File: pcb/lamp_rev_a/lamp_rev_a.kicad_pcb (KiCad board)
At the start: 4 copper layers, 100 x 80 mm, 0 parts

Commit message: Materialize LAMP Rev A KiCad board
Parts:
- added C1: 22uF, lcsc:C1206, F.Cu at (26.0, 8.00)
- added C10: 100nF, lcsc:C0603, F.Cu at (42.0, 14.0)
- added C11: 100nF, lcsc:C0603, F.Cu at (47.0, 14.0)
- added C12: 100nF, lcsc:C0603, F.Cu at (50.0, 51.0)
- added C13: 100nF, lcsc:C0603, F.Cu at (54.0, 51.0)
- added C14: 100nF, lcsc:C0603, F.Cu at (44.0, 55.0)
- added C15: 100nF, lcsc:C0603, F.Cu at (68.0, 15.0)
- added C16: 100nF, lcsc:C0603, F.Cu at (9.00, 57.0)
- added C17: 100nF, lcsc:C0603, F.Cu at (21.0, 57.0)
- added C18: 100nF, lcsc:C0603, F.Cu at (33.0, 57.0)
- added C19: 100nF, lcsc:C0603, F.Cu at (45.0, 68.0)
- added C2: 22uF, lcsc:C1206, F.Cu at (38.0, 8.00)
- added C20: 100nF, lcsc:C0603, F.Cu at (69.0, 57.0)
- added C21: 100nF, lcsc:C0603, F.Cu at (93.0, 57.0)
- added C3: 22uF, lcsc:C1206, F.Cu at (48.0, 12.0)
- added C4: 22uF, lcsc:C1206, F.Cu at (84.0, 6.00)
- added C5: 10pF, lcsc:C0603, F.Cu at (47.0, 62.0)
- added C6: 100nF, lcsc:C0603, F.Cu at (18.0, 14.0)
- added C7: 100nF, lcsc:C0603, F.Cu at (22.0, 14.0)
- added C8: 100nF, lcsc:C0603, F.Cu at (27.0, 18.0)
- added C9: 100nF, lcsc:C0603, F.Cu at (17.0, 9.00)
- added D1: SS34, lcsc:SMA_L4.3-W2.6-LS5.2-RD, F.Cu at (32.0, 8.00)
- added D10: SMBJ18A, lcsc:SMB_L4.6-W3.6-LS5.3-RD, F.Cu at (75.0, 25.0)
- added D11: KT-0603R, lcsc:LED0603-RD, F.Cu at (10.0, 30.0)
- added D12: KT-0603R, lcsc:LED0603-RD, F.Cu at (15.0, 30.0)
- added D13: SS34, lcsc:SMA_L4.3-W2.6-LS5.2-RD, F.Cu at (84.0, 12.0)
- added D2: KT-0603R, lcsc:LED0603-RD, F.Cu at (8.00, 54.0)
- added D3: KT-0603R, lcsc:LED0603-RD, F.Cu at (20.0, 54.0)
- added D4: KT-0603R, lcsc:LED0603-RD, F.Cu at (32.0, 54.0)
- added D5: KT-0603R, lcsc:LED0603-RD, F.Cu at (44.0, 54.0)
- added D6: KT-0603R, lcsc:LED0603-RD, F.Cu at (56.0, 54.0)
- added D7: KT-0603R, lcsc:LED0603-RD, F.Cu at (68.0, 54.0)
- added D8: KT-0603R, lcsc:LED0603-RD, F.Cu at (80.0, 54.0)
- added D9: KT-0603R, lcsc:LED0603-RD, F.Cu at (92.0, 54.0)
- added F1: SMD2920-300C-36V, lcsc:FUSE2920, F.Cu at (82.0, 20.0)
- added J1: TYPE-C 3.1 MT 16P, lcsc:USB-C-SMD_TYPE-C-USB-4, F.Cu at (7.00, 7.00)
- added J2: DC-005-5A-2.0, lcsc:DC-IN-TH_DC-005-5A-2.0, F.Cu at (92.0, 8.00)
- added J3: DB128H-5.08-2P-BK-S, lcsc:TERM-BLOCK-5.08-2P, F.Cu at (92.0, 25.0)
- added PD1: SFH2704, lcsc:PHOTODIODE-SMD-2X1.8, F.Cu at (8.00, 70.0)
- added PD2: SFH2704, lcsc:PHOTODIODE-SMD-2X1.8, F.Cu at (20.0, 70.0)
- added PD3: SFH2704, lcsc:PHOTODIODE-SMD-2X1.8, F.Cu at (32.0, 70.0)
- added PD4: SFH2704, lcsc:PHOTODIODE-SMD-2X1.8, F.Cu at (44.0, 70.0)
- added PD5: SFH2704, lcsc:PHOTODIODE-SMD-2X1.8, F.Cu at (56.0, 70.0)
- added PD6: SFH2704, lcsc:PHOTODIODE-SMD-2X1.8, F.Cu at (68.0, 70.0)
- added PD7: SFH2704, lcsc:PHOTODIODE-SMD-2X1.8, F.Cu at (80.0, 70.0)
- added PD8: SFH2704, lcsc:PHOTODIODE-SMD-2X1.8, F.Cu at (92.0, 70.0)
- added Q1: AO3400A, lcsc:SOT-23-3_L2.9-W1.3-P1.90-LS2.4-BR, F.Cu at (75.0, 17.0)
- added Q2: MMBT3904, lcsc:SOT-23-3_L2.9-W1.3-P1.90-LS2.4-BR, F.Cu at (8.00, 48.0)
- added Q3: MMBT3904, lcsc:SOT-23-3_L2.9-W1.3-P1.90-LS2.4-BR, F.Cu at (20.0, 48.0)
- added Q4: MMBT3904, lcsc:SOT-23-3_L2.9-W1.3-P1.90-LS2.4-BR, F.Cu at (32.0, 48.0)
- added Q5: MMBT3904, lcsc:SOT-23-3_L2.9-W1.3-P1.90-LS2.4-BR, F.Cu at (44.0, 48.0)
- added Q6: MMBT3904, lcsc:SOT-23-3_L2.9-W1.3-P1.90-LS2.4-BR, F.Cu at (56.0, 48.0)
- added Q7: MMBT3904, lcsc:SOT-23-3_L2.9-W1.3-P1.90-LS2.4-BR, F.Cu at (68.0, 48.0)
- added Q8: MMBT3904, lcsc:SOT-23-3_L2.9-W1.3-P1.90-LS2.4-BR, F.Cu at (80.0, 48.0)
- added Q9: MMBT3904, lcsc:SOT-23-3_L2.9-W1.3-P1.90-LS2.4-BR, F.Cu at (92.0, 48.0)
- added R1: 5.1k, lcsc:R0805, F.Cu at (12.0, 13.0)
- added R10: 100R, lcsc:R0805, F.Cu at (80.0, 51.0)
- added R11: 100R, lcsc:R0805, F.Cu at (92.0, 51.0)
- added R12: 1k, lcsc:R0805, F.Cu at (8.00, 46.0)
- added R13: 1k, lcsc:R0805, F.Cu at (20.0, 46.0)
- added R14: 1k, lcsc:R0805, F.Cu at (32.0, 46.0)
- added R15: 1k, lcsc:R0805, F.Cu at (44.0, 46.0)
- added R16: 1k, lcsc:R0805, F.Cu at (56.0, 46.0)
- added R17: 1k, lcsc:R0805, F.Cu at (68.0, 46.0)
- added R18: 1k, lcsc:R0805, F.Cu at (80.0, 46.0)
- added R19: 1k, lcsc:R0805, F.Cu at (92.0, 46.0)
- added R2: 5.1k, lcsc:R0805, F.Cu at (12.0, 15.0)
- added R20: 1k, lcsc:R0805, F.Cu at (10.0, 27.0)
- added R21: 1k, lcsc:R0805, F.Cu at (15.0, 27.0)
- added R22: 4.7k, lcsc:R0805, F.Cu at (29.0, 28.0)
- added R23: 4.7k, lcsc:R0805, F.Cu at (32.0, 28.0)
- added R24: 10k, lcsc:R0805, F.Cu at (26.0, 24.0)
- added R25: 10k, lcsc:R0805, F.Cu at (30.0, 24.0)
- added R26: 10k, lcsc:R0805, F.Cu at (57.0, 50.0)
- added R27: 10k, lcsc:R0805, F.Cu at (60.0, 50.0)
- added R28: 10k, lcsc:R0805, F.Cu at (65.0, 50.0)
- added R29: 10k, lcsc:R0805, F.Cu at (68.0, 50.0)
- added R3: 1M, lcsc:R0805, F.Cu at (43.0, 62.0)
- added R4: 100R, lcsc:R0805, F.Cu at (8.00, 51.0)
- added R5: 100R, lcsc:R0805, F.Cu at (20.0, 51.0)
- added R6: 100R, lcsc:R0805, F.Cu at (32.0, 51.0)
- added R7: 100R, lcsc:R0805, F.Cu at (44.0, 51.0)
- added R8: 100R, lcsc:R0805, F.Cu at (56.0, 51.0)
- added R9: 100R, lcsc:R0805, F.Cu at (68.0, 51.0)
- added TP_12V: +12V_RAW, lcsc:TESTPOINT_SMD_1.5MM, F.Cu at (98.0, 5.00)
- added TP_3V3: +3V3, lcsc:TESTPOINT_SMD_1.5MM, F.Cu at (50.0, 4.00)
- added TP_5V: +5V, lcsc:TESTPOINT_SMD_1.5MM, F.Cu at (38.0, 4.00)
- added TP_ADC: ADC_AIN1, lcsc:TESTPOINT_SMD_1.5MM, F.Cu at (40.0, 74.0)
- added TP_BOOT: ESP_GPIO0, lcsc:TESTPOINT_SMD_1.5MM, F.Cu at (22.0, 34.0)
- added TP_EN: ESP_EN, lcsc:TESTPOINT_SMD_1.5MM, F.Cu at (18.0, 34.0)
- added TP_GND: GND, lcsc:TESTPOINT_SMD_1.5MM, F.Cu at (5.00, 38.0)
- added TP_HEATER: HEATER_P, lcsc:TESTPOINT_SMD_1.5MM, F.Cu at (98.0, 30.0)
- added TP_HEATER_SUPPLY: HEATER_SUPPLY, lcsc:TESTPOINT_SMD_1.5MM, F.Cu at (88.0, 34.0)
- added TP_MUX: MUX_COM, lcsc:TESTPOINT_SMD_1.5MM, F.Cu at (45.0, 74.0)
- added TP_PWM: HEATER_PWM, lcsc:TESTPOINT_SMD_1.5MM, F.Cu at (64.0, 4.00)
- added TP_RX: UART_RX, lcsc:TESTPOINT_SMD_1.5MM, F.Cu at (30.0, 34.0)
- added TP_SCL: SCL, lcsc:TESTPOINT_SMD_1.5MM, F.Cu at (32.0, 34.0)
- added TP_SDA: SDA, lcsc:TESTPOINT_SMD_1.5MM, F.Cu at (28.0, 34.0)
- added TP_TX: UART_TX, lcsc:TESTPOINT_SMD_1.5MM, F.Cu at (26.0, 34.0)
- added TP_VBUS: VBUS, lcsc:TESTPOINT_SMD_1.5MM, F.Cu at (12.0, 4.00)
- added U1: ESP32-S3-WROOM-1-N8, lcsc:WIFIM-SMD_ESP32-S3-WROOM-1-N8, F.Cu at (22.0, 20.0)
- added U2: USBLC6-2SC6, lcsc:SOT-23-6, F.Cu at (17.0, 8.00)
- added U3: AMS1117-3.3, lcsc:SOT-223, F.Cu at (44.0, 10.0)
- added U4: ADS1115IDGSR, lcsc:MSOP-10_L3.0-W3.0-P0.50-LS5.0-BL, F.Cu at (50.0, 48.0)
- added U5: CD74HC4051M, lcsc:SOIC-16_L9.9-W3.9-P1.27-LS6.0-BL, F.Cu at (52.0, 58.0)
- added U6: TLV6001IDBVR, lcsc:SOT-23-5, F.Cu at (43.0, 58.0)
- added U7: TC4427ACOA, lcsc:SOIC-8_L4.9-W3.9-P1.27-LS6.0-BL, F.Cu at (68.0, 12.0)
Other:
- board text added: "S0"
- board text added: "S1"
- board text added: "S2"
- board text added: "S3"
- board text added: "S4"
- board text added: "S5"
- board text added: "S6"
- board text added: "S7"
- board text added: "analog_optical: LED emitters, photodiodes, mux, ADC, guarded analog routes"
- board text added: "heater_power: 12 V input, heater connector, MOSFET, gate driver, current-return path"
- board text added: "low_voltage_power: USB-derived 5 V, 3.3 V regulation, rail bulk capacitance"
- board text added: "mcu_usb: ESP32-S3 module, USB-C, boot/reset, UART/JTAG/debug"
- board text added: "mechanical_thermal: Heater block mounts, tube geometry, enclosure mounting holes"

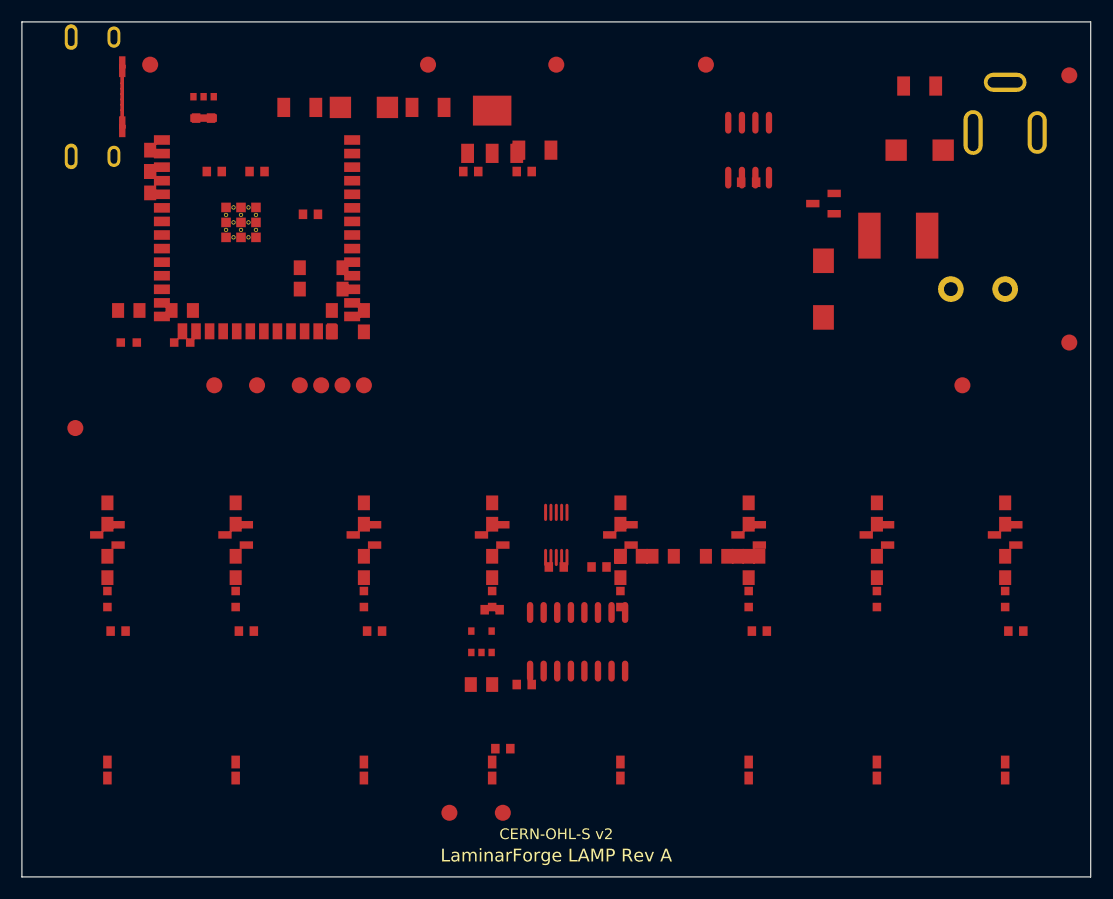
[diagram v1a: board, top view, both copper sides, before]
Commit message: Add LAMP Rev A pin net assignments
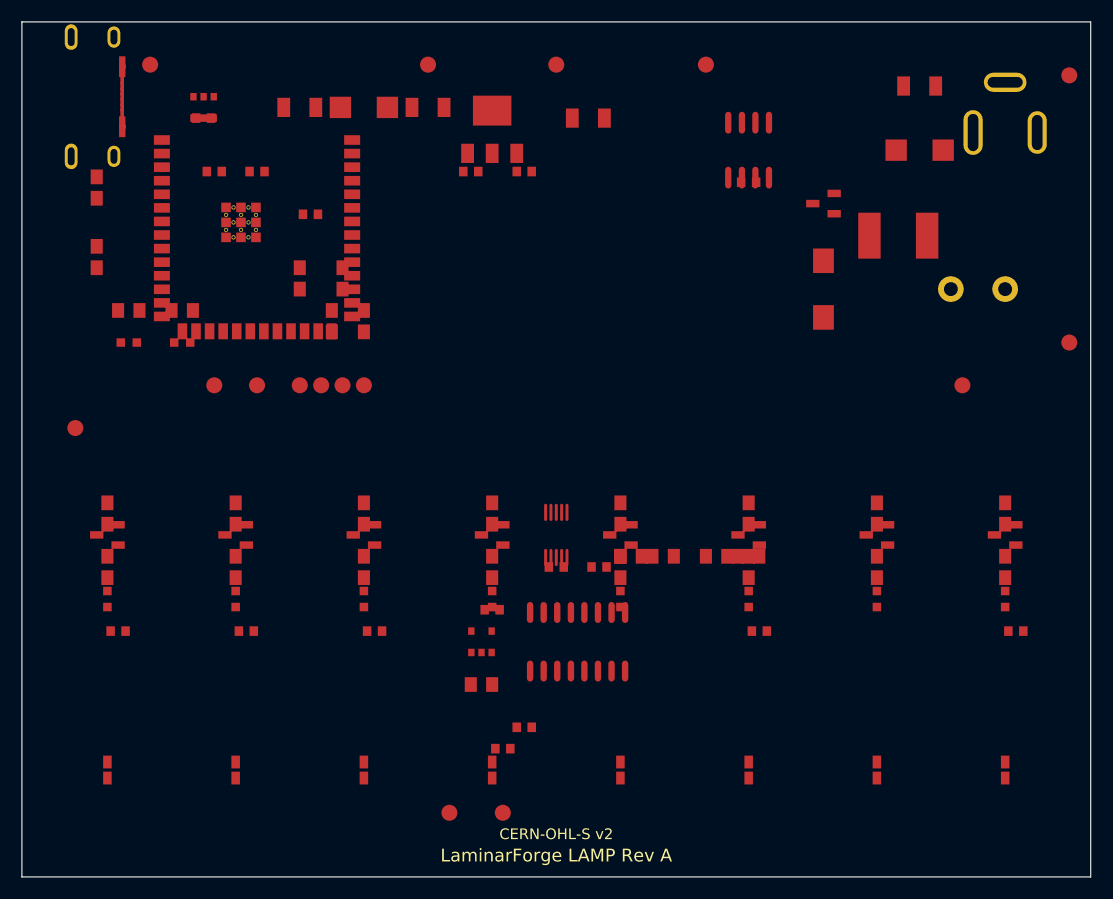
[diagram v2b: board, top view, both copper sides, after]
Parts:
- moved R2 8.60 mm to (7.00, 22.0)
- moved C3 5.83 mm to (53.0, 9.00)
- moved R1 5.59 mm to (7.00, 15.5)
- moved C5 4.00 mm to (47.0, 66.0)
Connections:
- C1 pad 1: (no net) -> VBUS
- C1 pad 2: (no net) -> GND
- C2 pad 1: (no net) -> +5V
- C2 pad 2: (no net) -> GND
- C3 pad 1: (no net) -> +3V3
- C3 pad 2: (no net) -> GND
- C4 pad 1: (no net) -> +12V_RAW
- C4 pad 2: (no net) -> GND
- C5 pad 1: (no net) -> MUX_COM
- C5 pad 2: (no net) -> ADC_AIN1
- D1 pad 1: (no net) -> VBUS
- D1 pad 2: (no net) -> +5V
- D10 pad 1: (no net) -> HEATER_SUPPLY
- D10 pad 2: (no net) -> GND
- D13 pad 1: (no net) -> +12V_RAW
- D13 pad 2: (no net) -> +12V
- F1 pad 1: (no net) -> +12V
- F1 pad 2: (no net) -> HEATER_SUPPLY
- J1 pad 13: (no net) -> GND
- J1 pad 14: (no net) -> GND
- J1 pad 15: (no net) -> GND
- J1 pad 16: (no net) -> GND
- J1 pad A12B1: (no net) -> GND
- J1 pad A5: (no net) -> USB_CC1
- J1 pad A6: (no net) -> USB_DP
- J1 pad A7: (no net) -> USB_DN
- J1 pad A9B4: (no net) -> VBUS
- J1 pad B12A1: (no net) -> GND
- J1 pad B5: (no net) -> USB_CC2
- J1 pad B6: (no net) -> USB_DP
- J1 pad B7: (no net) -> USB_DN
- J1 pad B9A4: (no net) -> VBUS
- J2 pad 1: (no net) -> +12V_RAW
- J2 pad 2: (no net) -> GND
- J2 pad 3: (no net) -> GND
- J3 pad 1: (no net) -> HEATER_SUPPLY
- J3 pad 2: (no net) -> HEATER_P
- Q1 pad 1: (no net) -> GATE_DRV
- Q1 pad 2: (no net) -> GND
- Q1 pad 3: (no net) -> HEATER_P
- R1 pad 1: (no net) -> USB_CC1
- R1 pad 2: (no net) -> GND
- R2 pad 1: (no net) -> USB_CC2
- R2 pad 2: (no net) -> GND
- R3 pad 1: (no net) -> MUX_COM
- R3 pad 2: (no net) -> ADC_AIN1
- U1 pad 1: (no net) -> GND
- U1 pad 13: (no net) -> USB_DN
- U1 pad 14: (no net) -> USB_DP
- U1 pad 15: (no net) -> HEATER_PWM
- U1 pad 16: (no net) -> SDA
- U1 pad 17: (no net) -> SCL
- U1 pad 18: (no net) -> MUX_S0
- U1 pad 19: (no net) -> MUX_S1
- U1 pad 2: (no net) -> +3V3
- U1 pad 20: (no net) -> MUX_S2
- U1 pad 21: (no net) -> LED_BASE_0
- U1 pad 22: (no net) -> LED_BASE_1
- U1 pad 23: (no net) -> LED_BASE_2
- U1 pad 24: (no net) -> LED_BASE_3
- U1 pad 25: (no net) -> LED_BASE_4
- U1 pad 26: (no net) -> LED_BASE_5
- U1 pad 27: (no net) -> ESP_GPIO0
- U1 pad 28: (no net) -> LED_BASE_7
- U1 pad 3: (no net) -> ESP_EN
- U1 pad 30: (no net) -> LED_BASE_6
- U1 pad 35: (no net) -> ESP_GPIO_ACT
- U1 pad 36: (no net) -> UART_RX
- U1 pad 37: (no net) -> UART_TX
- U1 pad 41: (no net) -> GND
- U2 pad 1: (no net) -> USB_DP
- U2 pad 2: (no net) -> GND
- U2 pad 3: (no net) -> USB_DN
- U2 pad 4: (no net) -> USB_DN
- U2 pad 5: (no net) -> VBUS
- U2 pad 6: (no net) -> USB_DP
- U3 pad 1: (no net) -> GND
- U3 pad 2: (no net) -> +3V3
- U3 pad 3: (no net) -> +5V
- U3 pad 4: (no net) -> +3V3
- U4 pad 1: (no net) -> GND
- U4 pad 10: (no net) -> SCL
- U4 pad 3: (no net) -> GND
- U4 pad 4: (no net) -> ADC_AIN1
- U4 pad 8: (no net) -> +3V3
- U4 pad 9: (no net) -> SDA
- U5 pad 1: (no net) -> MUX_Y4
- U5 pad 10: (no net) -> MUX_S1
- U5 pad 11: (no net) -> MUX_S0
- U5 pad 12: (no net) -> MUX_Y3
- U5 pad 13: (no net) -> MUX_Y0
- U5 pad 14: (no net) -> MUX_Y1
- U5 pad 15: (no net) -> MUX_Y2
- U5 pad 16: (no net) -> +3V3
- U5 pad 2: (no net) -> MUX_Y6
- U5 pad 3: (no net) -> MUX_COM
- U5 pad 4: (no net) -> MUX_Y7
- U5 pad 5: (no net) -> MUX_Y5
- U5 pad 6: (no net) -> GND
- U5 pad 7: (no net) -> GND
- U5 pad 8: (no net) -> GND
- U5 pad 9: (no net) -> MUX_S2
- U6 pad 1: (no net) -> ADC_AIN1
- U6 pad 2: (no net) -> GND
- U6 pad 3: (no net) -> GND
- U6 pad 4: (no net) -> MUX_COM
- U6 pad 5: (no net) -> +3V3
- U7 pad 2: (no net) -> HEATER_PWM
- U7 pad 3: (no net) -> GND
- U7 pad 6: (no net) -> +12V
- U7 pad 7: (no net) -> GATE_DRV

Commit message: Clean PCB outputs and stabilize LAMP Rev A placement
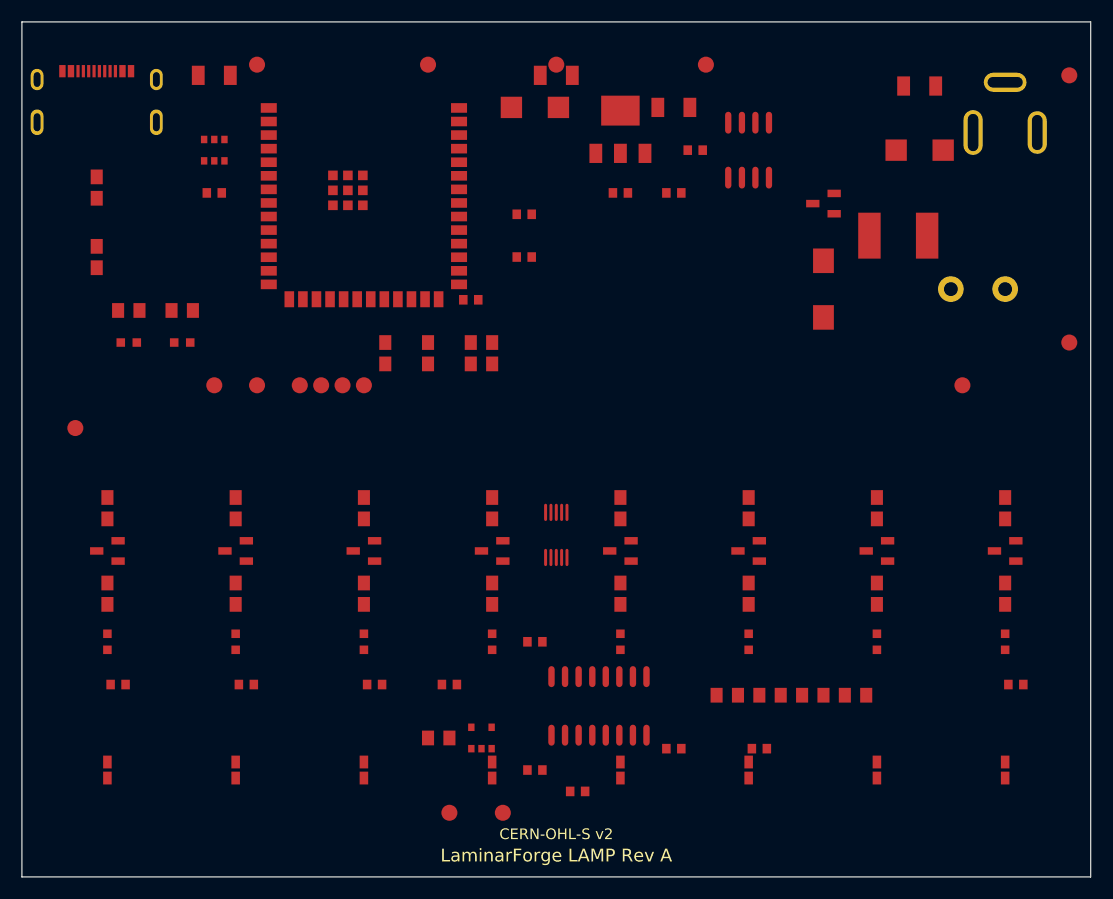
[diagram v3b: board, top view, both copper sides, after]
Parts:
- removed the C10 at (42.0, 14.0)
- removed the C11 at (47.0, 14.0)
- removed the C12 at (50.0, 51.0)
- removed the C13 at (54.0, 51.0)
- removed the C14 at (44.0, 55.0)
- removed the C15 at (68.0, 15.0)
- removed the C16 at (9.00, 57.0)
- removed the C17 at (21.0, 57.0)
- removed the C18 at (33.0, 57.0)
- removed the C19 at (45.0, 68.0)
- removed the C20 at (69.0, 57.0)
- removed the C21 at (93.0, 57.0)
- removed the C7 at (22.0, 14.0)
- removed the C8 at (27.0, 18.0)
- removed the C9 at (17.0, 9.00)
- removed the TP_5V at (38.0, 4.00)
- added R13: 1k, lcsc:R0805, F.Cu at (20.0, 45.5)
- added R14: 1k, lcsc:R0805, F.Cu at (32.0, 45.5)
- added R15: 1k, lcsc:R0805, F.Cu at (44.0, 45.5)
- added R16: 1k, lcsc:R0805, F.Cu at (56.0, 45.5)
- added R17: 1k, lcsc:R0805, F.Cu at (68.0, 45.5)
- added R18: 1k, lcsc:R0805, F.Cu at (80.0, 45.5)
- added R19: 1k, lcsc:R0805, F.Cu at (92.0, 45.5)
- added R20: 1k, lcsc:R0805, F.Cu at (10.0, 27.0)
- added R21: 1k, lcsc:R0805, F.Cu at (15.0, 27.0)
- added R22: 4.7k, lcsc:R0805, F.Cu at (34.0, 31.0)
- added R23: 4.7k, lcsc:R0805, F.Cu at (38.0, 31.0)
- added R24: 10k, lcsc:R0805, F.Cu at (42.0, 31.0)
- added R25: 10k, lcsc:R0805, F.Cu at (44.0, 31.0)
- added R26: 10k, lcsc:R0805, F.Cu at (66.0, 63.0)
- added R27: 10k, lcsc:R0805, F.Cu at (70.0, 63.0)
- added R28: 10k, lcsc:R0805, F.Cu at (74.0, 63.0)
- C10: renamed from R18; value 1k -> 100nF; footprint lcsc:R0805 -> lcsc:C0603
- C11: renamed from R19; value 1k -> 100nF; footprint lcsc:R0805 -> lcsc:C0603
- C12: renamed from R20; value 1k -> 100nF; footprint lcsc:R0805 -> lcsc:C0603
- C13: renamed from R21; value 1k -> 100nF; footprint lcsc:R0805 -> lcsc:C0603
- C14: renamed from R22; value 4.7k -> 100nF; footprint lcsc:R0805 -> lcsc:C0603
- C15: renamed from R23; value 4.7k -> 100nF; footprint lcsc:R0805 -> lcsc:C0603
- C16: renamed from R24; value 10k -> 100nF; footprint lcsc:R0805 -> lcsc:C0603
- C17: renamed from R25; value 10k -> 100nF; footprint lcsc:R0805 -> lcsc:C0603
- C18: renamed from R26; value 10k -> 100nF; footprint lcsc:R0805 -> lcsc:C0603
- C19: renamed from R27; value 10k -> 100nF; footprint lcsc:R0805 -> lcsc:C0603
- C20: renamed from R28; value 10k -> 100nF; footprint lcsc:R0805 -> lcsc:C0603
- C21: renamed from R29; value 10k -> 100nF; footprint lcsc:R0805 -> lcsc:C0603
- C6: renamed from R14; value 1k -> 100nF; footprint lcsc:R0805 -> lcsc:C0603
- C7: renamed from R15; value 1k -> 100nF; footprint lcsc:R0805 -> lcsc:C0603
- C8: renamed from R16; value 1k -> 100nF; footprint lcsc:R0805 -> lcsc:C0603
- C9: renamed from R17; value 1k -> 100nF; footprint lcsc:R0805 -> lcsc:C0603
- R29: renamed from R13; value 1k -> 10k
- TP_5V: renamed from C6; value 100nF -> +5V; footprint lcsc:C0603 -> lcsc:TESTPOINT_SMD_1.5MM
- moved C13 61.6 mm to (61.0, 68.0)
- moved R29 60.4 mm to (78.0, 63.0), turned to 0 degrees
- moved C9 58.3 mm to (18.0, 16.0), turned to 0 degrees
- moved C12 46.1 mm to (40.0, 62.0)
- moved C11 43.1 mm to (61.0, 16.0), turned to 0 degrees
- moved C16 41.6 mm to (9.00, 62.0), turned to 0 degrees
- moved C17 39.1 mm to (21.0, 62.0), turned to 0 degrees
- moved C10 38.4 mm to (56.0, 16.0), turned to 0 degrees
- moved C14 35.5 mm to (48.0, 58.0), turned to 0 degrees
- moved C15 34.9 mm to (63.0, 12.0), turned to 0 degrees
- moved C6 31.8 mm to (47.0, 18.0), turned to 0 degrees
- moved C21 27.7 mm to (93.0, 62.0)
- moved C18 26.8 mm to (33.0, 62.0)
- moved C8 24.4 mm to (42.0, 26.0), turned to 0 degrees
- moved C7 24.2 mm to (47.0, 22.0), turned to 0 degrees
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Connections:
- TP_5V pad 1: (no net) -> +5V
